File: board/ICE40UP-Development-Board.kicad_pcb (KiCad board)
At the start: 4 copper layers, 41.9 x 20.3 mm, 60 parts, among them X1 USB4105-GF-A, X2 Conn_01x16, X3 Conn_01x16, X4 Tag-Connect, Y1 48MHz

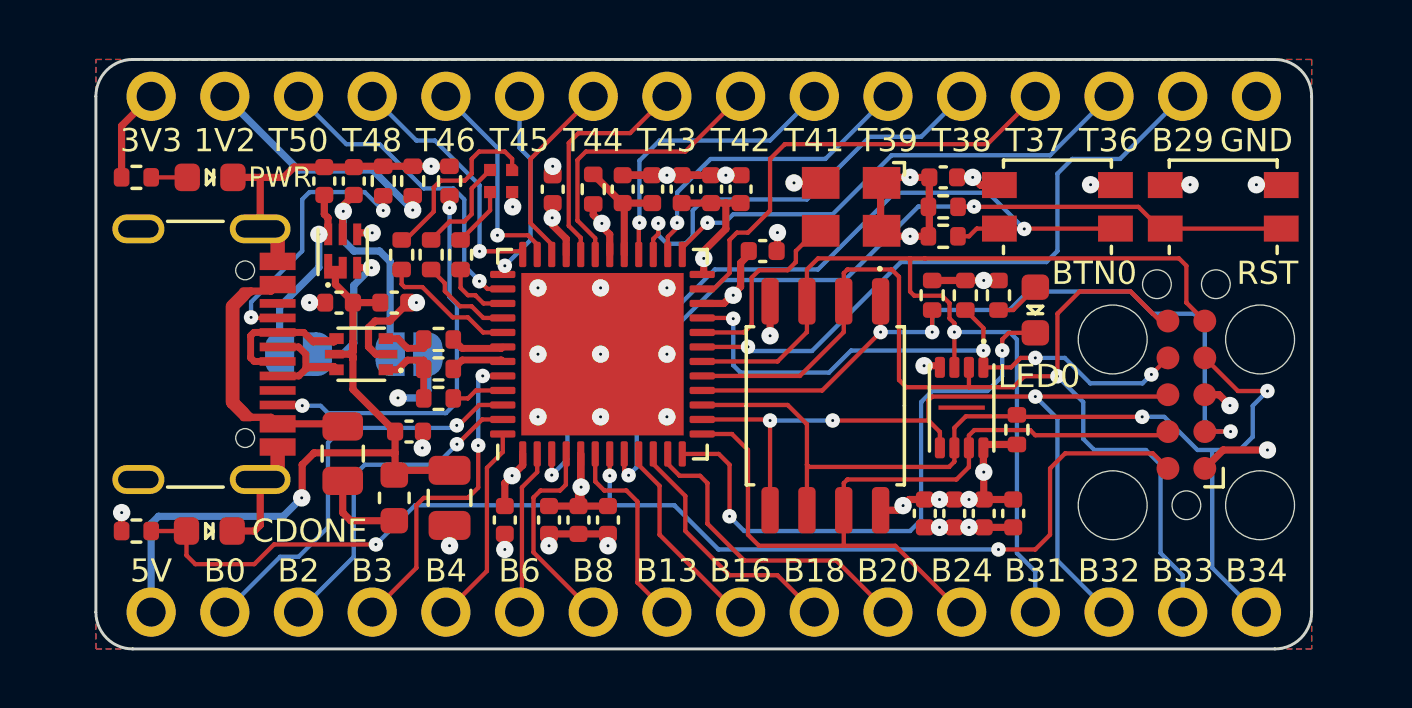
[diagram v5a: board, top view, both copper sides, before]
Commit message: change led resistor values
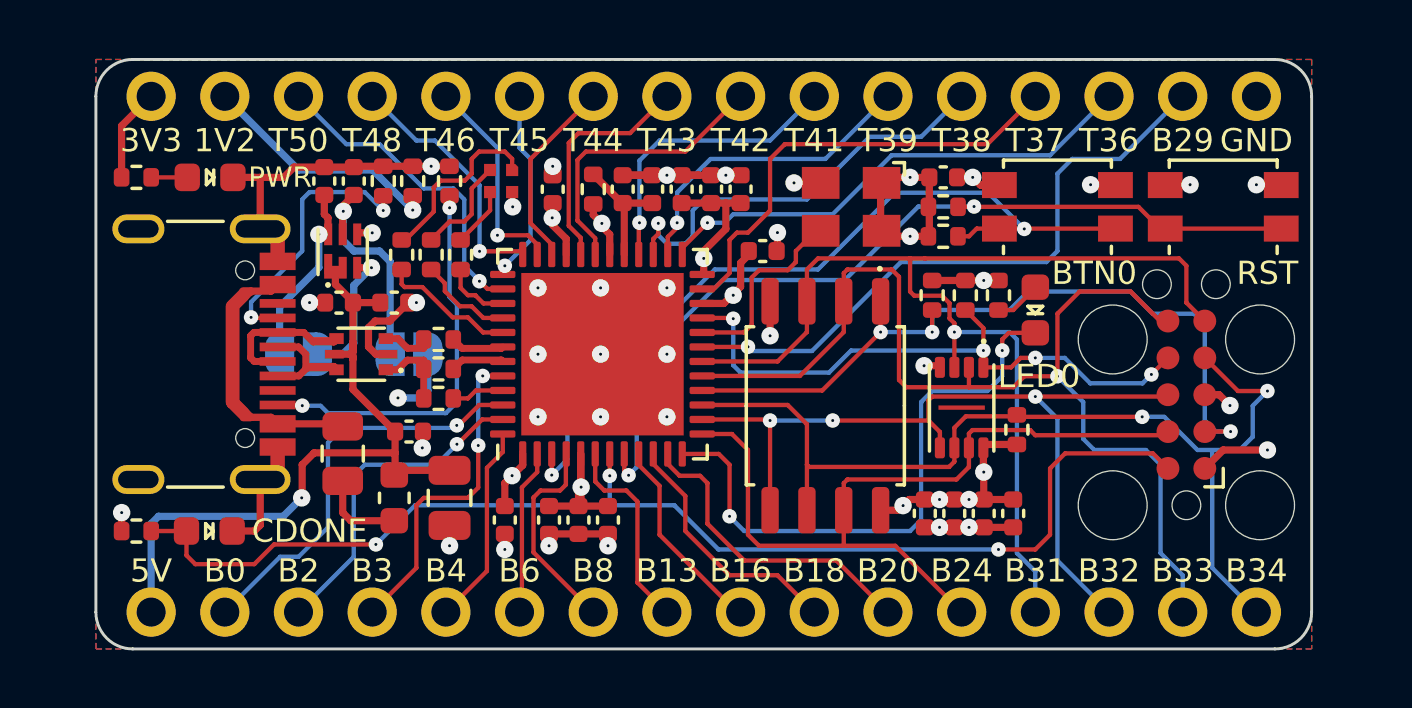
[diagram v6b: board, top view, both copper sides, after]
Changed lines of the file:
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@@
   (segment (start 77.47 94.488) (end 78.105 95.123) (width 0.15) (layer "B.Cu") (net 31))
   (segment (start 78.105 95.123) (end 78.105 96.52) (width 0.15) (layer "B.Cu") (net 31))
+  (segment (start 68.58 94.234) (end 73.279 94.234) (width 0.15) (layer "F.Cu") (net 32))
+  (segment (start 75.815 91.5202) (end 75.815 90.365751) (width 0.15) (layer "F.Cu") (net 32))
   (segment (start 71.628 91.948) (end 75.3872 91.948) (width 0.15) (layer "F.Cu") (net 32))
+  (segment (start 71.501 93.008) (end 71.501 92.075) (width 0.15) (layer "F.Cu") (net 32))
   (segment (start 78.105 90.424) (end 82.55 90.424) (width 0.15) (layer "F.Cu") (net 32))
-  (segment (start 75.999001 90.2465) (end 77.9275 90.2465) (width 0.15) (layer "F.Cu") (net 32))
-  (segment (start 68.58 94.234) (end 73.279 94.234) (width 0.15) (layer "F.Cu") (net 32))
-  (segment (start 75.3872 91.948) (end 75.815 91.5202) (width 0.15) (layer "F.Cu") (net 32))
   (segment (start 68.199 90.932) (end 68.199 93.853) (width 0.15) (layer "F.Cu") (net 32))
   (segment (start 68.199 93.853) (end 68.58 94.234) (width 0.15) (layer "F.Cu") (net 32))
-  (segment (start 75.815 91.5202) (end 75.815 90.430501) (width 0.15) (layer "F.Cu") (net 32))
+  (segment (start 75.815 90.365751) (end 75.934251 90.2465) (width 0.15) (layer "F.Cu") (net 32))
+  (segment (start 82.55 90.424) (end 82.677 90.297) (width 0.15) (layer "F.Cu") (net 32))
   (segment (start 67.647 90.38) (end 68.199 90.932) (width 0.15) (layer "F.Cu") (net 32))
-  (segment (start 71.501 92.075) (end 71.628 91.948) (width 0.15) (layer "F.Cu") (net 32))
   (segment (start 71.501 93.008) (end 71.501 94.234) (width 0.15) (layer "F.Cu") (net 32))
-  (segment (start 77.9275 90.2465) (end 78.105 90.424) (width 0.15) (layer "F.Cu") (net 32))
-  (segment (start 71.501 93.008) (end 71.501 92.075) (width 0.15) (layer "F.Cu") (net 32))
+  (segment (start 75.3872 91.948) (end 75.815 91.5202) (width 0.15) (layer "F.Cu") (net 32))
+  (segment (start 75.934251 90.2465) (end 77.9275 90.2465) (width 0.15) (layer "F.Cu") (net 32))
   (segment (start 66.6215 90.38) (end 67.647 90.38) (width 0.15) (layer "F.Cu") (net 32))
   (segment (start 73.279 94.234) (end 75.565 96.52) (width 0.15) (layer "F.Cu") (net 32))
-  (segment (start 75.815 90.430501) (end 75.999001 90.2465) (width 0.15) (layer "F.Cu") (net 32))
-  (segment (start 82.55 90.424) (end 82.677 90.297) (width 0.15) (layer "F.Cu") (net 32))
+  (segment (start 77.9275 90.2465) (end 78.105 90.424) (width 0.15) (layer "F.Cu") (net 32))
+  (segment (start 71.501 92.075) (end 71.628 91.948) (width 0.15) (layer "F.Cu") (net 32))
   (segment (start 60.406 92.220793) (end 60.406 96.439) (width 0.15) (layer "F.Cu") (net 33))
   (segment (start 60.406 96.439) (end 60.325 96.52) (width 0.15) (layer "F.Cu") (net 33))

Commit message: change tag-connect pinout; add reset signal to tag-connect
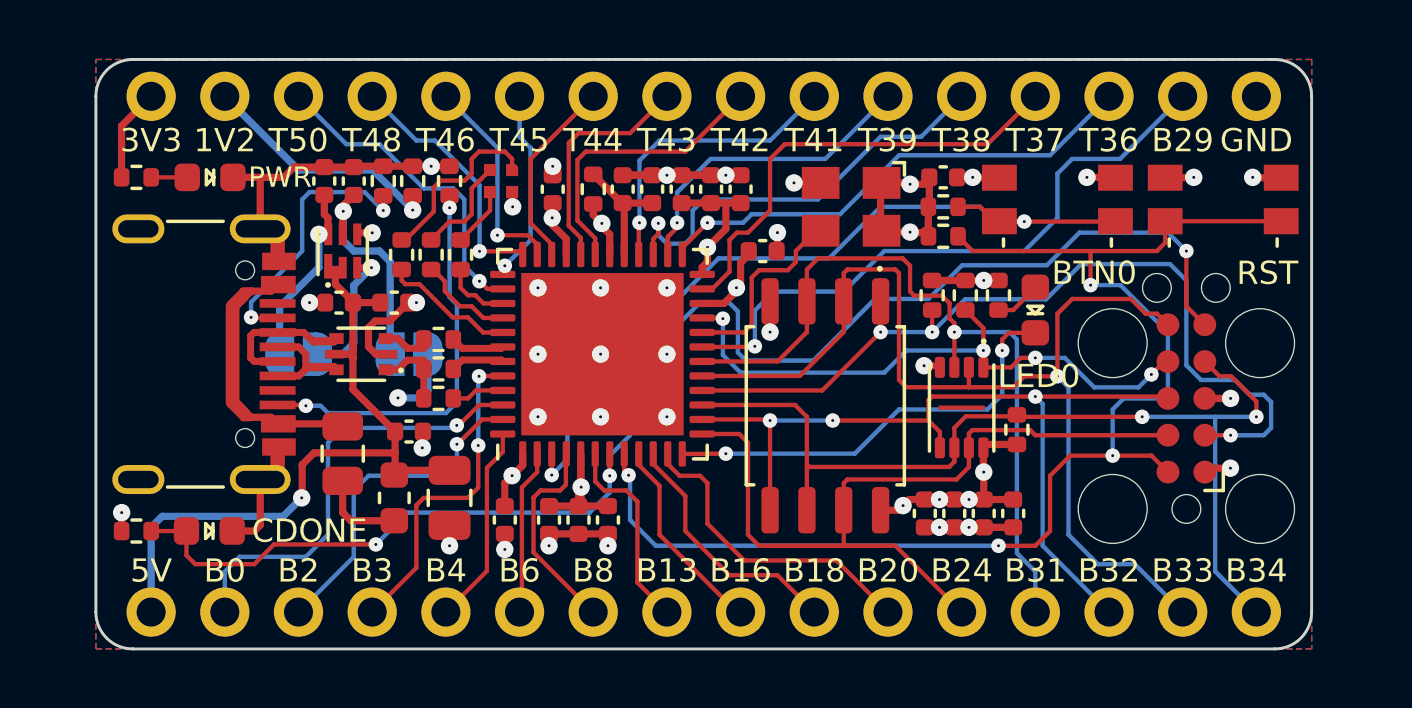
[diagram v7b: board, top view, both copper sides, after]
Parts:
- R16, R18: value 270R -> 10k
- R17: value 2k2 -> 10k
- moved R11 1.02 mm to (74.9, 82.5)
- moved R12 1.02 mm to (74.9, 83.6)
- moved S1 0.25 mm to (78.9, 82.3)
- moved S2 0.25 mm to (84.6, 82.3)
- moved X4 0.13 mm to (83.3, 89.2)
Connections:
- X4 pad 10: CDONE -> ~{RST}
- X4 pad 5: SPI_~{WP} -> CDONE
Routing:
- net ~{RST}: track 30.6 -> 46.6 mm, vias 2 -> 4
- net SPI_~{WP}: track 38.6 -> 26.6 mm
- net CDONE: track 42.2 -> 50.2 mm
- net CONF_O: track 20.3 -> 15.1 mm
- net FLASH_~{SS}: track 26.6 -> 30.3 mm
- net IOB_0a: track 14.3 -> 15.2 mm
- net SPI_SCK: track 35.0 -> 34.2 mm
- net +3V3: track 39.1 -> 38.3 mm
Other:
- board text added: "ICE40UP Dev Board"

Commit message: add back silkscreen
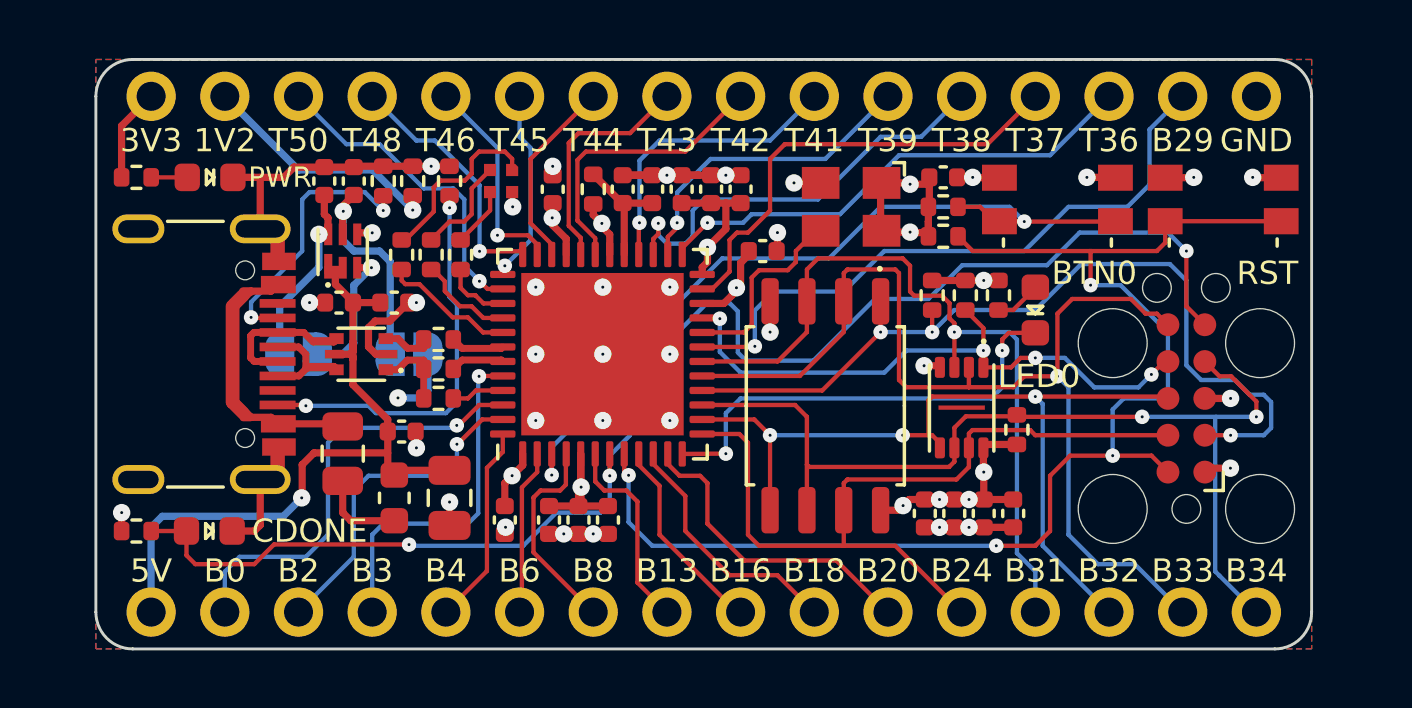
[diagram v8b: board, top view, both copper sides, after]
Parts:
- added REF**: OSHW-Logo_5.7x6mm_SilkScreen, Symbol:OSHW-Logo_5.7x6mm_SilkScreen, B.Cu at (71.2, 90.3)
- moved C5 0.25 mm to (56.3, 90.3)
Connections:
- V2 pad 9: (no net) -> unconnected-(V2-NC-Pad9)
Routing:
- net IOB_3b: track 11.4 -> 12.2 mm, vias 2 -> 1
- net GND: track 43.6 -> 42.9 mm
- net CONF_O: track 15.1 -> 15.7 mm
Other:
- board text added: "Dev Board"
- board text added: "ICE40UP"
- board text added: "v1.0"
- board text removed: "ICE40UP Dev Board"
